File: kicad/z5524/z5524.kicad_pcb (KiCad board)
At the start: 4 copper layers, 80 x 80 mm, 210 parts, among them J1 Conn_01x01, J2 Conn_01x02, J3 Conn_02x20_Odd_Even, Q1 2N7002K, U1 TL074, U10 TL072, U11 NE5532, U12 TL074, U13 AS3364, U14 AD5328, U15 M24C02-WMN, U16 SSI2130, U17 DG442xY, U18 TL072, U19 LM311, U2 LM337L_TO92, U21 AD5328, U3 LM4040BIM3-2.5, U4 LM4040BIM3-4.1, U5 DG442xY, U6 TL072, U7 PCA9555D, U8 LM78L05_TO92, U9 AS3394

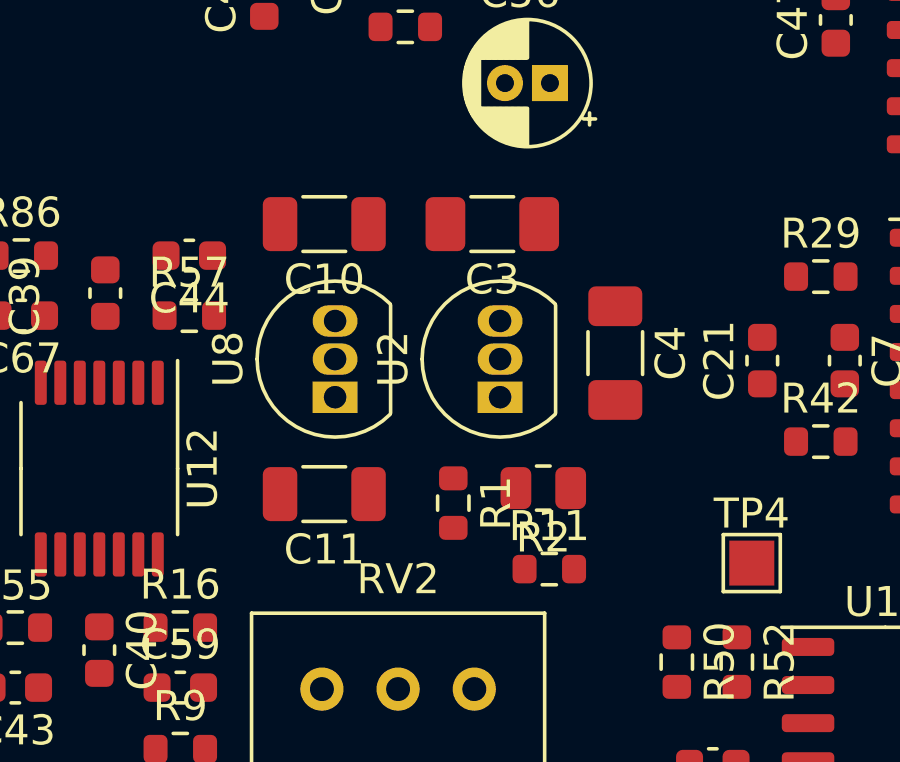
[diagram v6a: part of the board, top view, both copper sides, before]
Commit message: change some nets
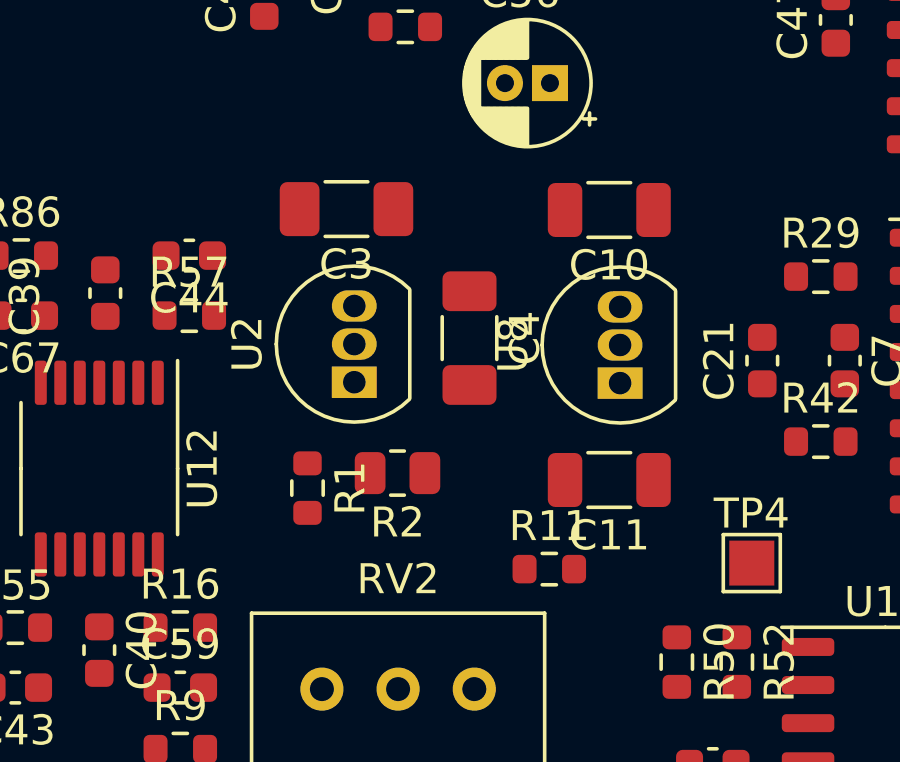
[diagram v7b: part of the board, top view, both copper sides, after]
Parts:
- moved C10 9.51 mm to (102.4, 53.4)
- moved C11 9.51 mm to (102.4, 62.4)
- moved U8 9.51 mm to (102.8, 59.2)
- moved C3 4.89 mm to (93.6, 53.4)
- moved C4 4.89 mm to (97.7, 57.7)
- moved R1 4.89 mm to (92.3, 62.7)
- moved R2 4.89 mm to (95.3, 62.2)
- moved U2 4.89 mm to (93.9, 59.2)
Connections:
- U21 pad 10: /DAC 2130/PULSE_MIX_DAC -> /DAC 2130/AS3394_VCO_CV_DAC
- U21 pad 11: /DAC 2130/TRI_MIX_DAC -> /DAC 2130/AS3394_SINE_CV_DAC
- U21 pad 12: /DAC 2130/AS3394_VCO_CV_DAC -> /DAC 2130/PULSE_MIX_DAC
- U21 pad 13: /DAC 2130/AS3394_SINE_CV_DAC -> /DAC 2130/TRI_MIX_DAC
- U21 pad 4: /DAC 2130/PWM_DAC -> /DAC 2130/SAW_MIX_DAC
- U21 pad 5: /DAC 2130/SAW_MIX_DAC -> /DAC 2130/LINEAR_DAC
- U21 pad 6: /DAC 2130/LINEAR_DAC -> /DAC 2130/EXP_PITCH_DAC
- U21 pad 7: /DAC 2130/EXP_PITCH_DAC -> /DAC 2130/PWM_DAC
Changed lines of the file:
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@@
   )
   (footprint "Resistor_SMD:R_0603_1608Metric" (layer "F.Cu")
-    (at 97.2 63.2 -90)
+    (at 92.34 62.7 -90)
     (descr "Resistor SMD 0603 (1608 Metric), square (rectangular) end terminal, IPC_7351 nominal, (Body size source: IPC-SM-782 page 72, https://www.pcb-3d.com/wordpress/wp-content/uploads/ipc-sm-782a_amendment_1_and_2.pdf), generated with kicad-footprint-generator")
     (tags "resistor")
@@
       (net 7 "+5V") (pinfunction "VDD") (pintype "power_in"))
     (pad "4" smd roundrect (at -2.8625 -0.325) (size 1.475 0.4) (layers "F.Cu" "F.Paste" "F.Mask") (roundrect_rratio 0.25)
-      (net 106 "/DAC 2130/PWM_DAC") (pinfunction "VOUT_A") (pintype "output"))
+      (net 107 "/DAC 2130/SAW_MIX_DAC") (pinfunction "VOUT_A") (pintype "output"))
     (pad "5" smd roundrect (at -2.8625 0.325) (size 1.475 0.4) (layers "F.Cu" "F.Paste" "F.Mask") (roundrect_rratio 0.25)
-      (net 107 "/DAC 2130/SAW_MIX_DAC") (pinfunction "VOUT_B") (pintype "output"))
+      (net 145 "/DAC 2130/LINEAR_DAC") (pinfunction "VOUT_B") (pintype "output"))
     (pad "6" smd roundrect (at -2.8625 0.975) (size 1.475 0.4) (layers "F.Cu" "F.Paste" "F.Mask") (roundrect_rratio 0.25)
-      (net 145 "/DAC 2130/LINEAR_DAC") (pinfunction "VOUT_C") (pintype "output"))
+      (net 100 "/DAC 2130/EXP_PITCH_DAC") (pinfunction "VOUT_C") (pintype "output"))
     (pad "7" smd roundrect (at -2.8625 1.625) (size 1.475 0.4) (layers "F.Cu" "F.Paste" "F.Mask") (roundrect_rratio 0.25)
-      (net 100 "/DAC 2130/EXP_PITCH_DAC") (pinfunction "VOUT_D") (pintype "output"))
+      (net 106 "/DAC 2130/PWM_DAC") (pinfunction "VOUT_D") (pintype "output"))
     (pad "8" smd roundrect (at -2.8625 2.275) (size 1.475 0.4) (layers "F.Cu" "F.Paste" "F.Mask") (roundrect_rratio 0.25)
       (net 5 "/VREF_2.5") (pinfunction "VREF_ABCD") (pintype "input"))
@@
       (net 5 "/VREF_2.5") (pinfunction "VREF_EFGH") (pintype "input"))
     (pad "10" smd roundrect (at 2.8625 1.625) (size 1.475 0.4) (layers "F.Cu" "F.Paste" "F.Mask") (roundrect_rratio 0.25)
-      (net 108 "/DAC 2130/PULSE_MIX_DAC") (pinfunction "VOUT_E") (pintype "output"))
+      (net 155 "/DAC 2130/AS3394_VCO_CV_DAC") (pinfunction "VOUT_E") (pintype "output"))
     (pad "11" smd roundrect (at 2.8625 0.975) (size 1.475 0.4) (layers "F.Cu" "F.Paste" "F.Mask") (roundrect_rratio 0.25)
-      (net 109 "/DAC 2130/TRI_MIX_DAC") (pinfunction "VOUT_F") (pintype "output"))
+      (net 156 "/DAC 2130/AS3394_SINE_CV_DAC") (pinfunction "VOUT_F") (pintype "output"))
     (pad "12" smd roundrect (at 2.8625 0.325) (size 1.475 0.4) (layers "F.Cu" "F.Paste" "F.Mask") (roundrect_rratio 0.25)
-      (net 155 "/DAC 2130/AS3394_VCO_CV_DAC") (pinfunction "VOUT_G") (pintype "output"))
+      (net 108 "/DAC 2130/PULSE_MIX_DAC") (pinfunction "VOUT_G") (pintype "output"))
     (pad "13" smd roundrect (at 2.8625 -0.325) (size 1.475 0.4) (layers "F.Cu" "F.Paste" "F.Mask") (roundrect_rratio 0.25)
-      (net 156 "/DAC 2130/AS3394_SINE_CV_DAC") (pinfunction "VOUT_H") (pintype "output"))
+      (net 109 "/DAC 2130/TRI_MIX_DAC") (pinfunction "VOUT_H") (pintype "output"))
     (pad "14" smd roundrect (at 2.8625 -0.975) (size 1.475 0.4) (layers "F.Cu" "F.Paste" "F.Mask") (roundrect_rratio 0.25)
       (net 1 "GND") (pinfunction "GND") (pintype "power_in"))
@@
   )
   (footprint "Capacitor_SMD:C_1206_3216Metric" (layer "F.Cu")
-    (at 92.9 62.9 180)
+    (at 102.4 62.43 180)
     (descr "Capacitor SMD 1206 (3216 Metric), square (rectangular) end terminal, IPC_7351 nominal, (Body size source: IPC-SM-782 page 76, https://www.pcb-3d.com/wordpress/wp-content/uploads/ipc-sm-782a_amendment_1_and_2.pdf), generated with kicad-footprint-generator")
     (tags "capacitor")
@@
   )
   (footprint "Package_TO_SOT_THT:TO-92_Inline" (layer "F.Cu")
-    (at 98.76 59.67 90)
+    (at 93.9 59.17 90)
     (descr "TO-92 leads in-line, narrow, oval pads, drill 0.75mm (see NXP sot054_po.pdf)")
     (tags "to-92 sc-43 sc-43a sot54 PA33 transistor")
@@
   )
   (footprint "Resistor_SMD:R_0805_2012Metric" (layer "F.Cu")
-    (at 100.2 62.7 180)
+    (at 95.34 62.2 180)
     (descr "Resistor SMD 0805 (2012 Metric), square (rectangular) end terminal, IPC_7351 nominal, (Body size source: IPC-SM-782 page 72, https://www.pcb-3d.com/wordpress/wp-content/uploads/ipc-sm-782a_amendment_1_and_2.pdf), generated with kicad-footprint-generator")
     (tags "resistor")
@@
   )
   (footprint "Capacitor_SMD:C_1206_3216Metric_Pad1.33x1.80mm_HandSolder" (layer "F.Cu")
-    (at 102.6 58.2 -90)
+    (at 97.74 57.7 -90)
     (descr "Capacitor SMD 1206 (3216 Metric), square (rectangular) end terminal, IPC_7351 nominal with elongated pad for handsoldering. (Body size source: IPC-SM-782 page 76, https://www.pcb-3d.com/wordpress/wp-content/uploads/ipc-sm-782a_amendment_1_and_2.pdf), generated with kicad-footprint-generator")
     (tags "capacitor handsolder")
@@
   )
   (footprint "Capacitor_SMD:C_1206_3216Metric_Pad1.33x1.80mm_HandSolder" (layer "F.Cu")
-    (at 98.5 53.9 180)
+    (at 93.64 53.4 180)
     (descr "Capacitor SMD 1206 (3216 Metric), square (rectangular) end terminal, IPC_7351 nominal with elongated pad for handsoldering. (Body size source: IPC-SM-782 page 76, https://www.pcb-3d.com/wordpress/wp-content/uploads/ipc-sm-782a_amendment_1_and_2.pdf), generated with kicad-footprint-generator")
     (tags "capacitor handsolder")
@@
   )
   (footprint "Capacitor_SMD:C_1206_3216Metric" (layer "F.Cu")
-    (at 92.9 53.9 180)
+    (at 102.4 53.43 180)
     (descr "Capacitor SMD 1206 (3216 Metric), square (rectangular) end terminal, IPC_7351 nominal, (Body size source: IPC-SM-782 page 76, https://www.pcb-3d.com/wordpress/wp-content/uploads/ipc-sm-782a_amendment_1_and_2.pdf), generated with kicad-footprint-generator")
     (tags "capacitor")
@@
   )
   (footprint "Package_TO_SOT_THT:TO-92_Inline" (layer "F.Cu")
-    (at 93.26 59.67 90)
+    (at 102.76 59.2 90)
     (descr "TO-92 leads in-line, narrow, oval pads, drill 0.75mm (see NXP sot054_po.pdf)")
     (tags "to-92 sc-43 sc-43a sot54 PA33 transistor")
@@
     )
   )
-  (group "" (id 2e246520-0b35-4792-ad25-97c2cddefbe2)
-    (members
-      92f9a68e-9e7e-466e-adbc-94ab08e4af57
-      d10bf185-8b68-491f-b0f1-91ced90c7d42
-    )
-  )
   (group "" (id 2fc85357-0847-4fe7-82a9-7b85cf4b86a6)
     (members
@@
     )
   )
-  (group "" (id 92f9a68e-9e7e-466e-adbc-94ab08e4af57)
+  (group "" (id 93d75bed-71db-44f9-b7da-dd2ff35bd6cd)
     (members
+      08c4fd51-5f1c-4dfa-ace4-9c1df0a83a9a
+      1761795b-03b3-4d1e-8c44-8f3a77735186
+      20aa8d9d-5e11-4ec8-bebb-96b6d7a66299
+      2b323b7b-dfb0-436f-9734-156e416652d1
+      32a03971-95b1-4e62-b42b-e4e30dc06bc9
       37a2353b-544e-489e-a308-03e152b14909
+      5a9364b0-aa06-471d-94c5-cc73b693e1fa
+      67ac6900-552f-4c0c-853a-365d1478a354
+      74f91626-498a-4694-b751-c8c8d0c3ce85
+      7aefe85a-953d-4bf9-832c-796f0bb3e17d
+      8c7152cb-4b92-4948-843e-82d814edd414
+      8d9b79bc-f815-4bc3-ab31-782ebc6dd427
+      a4beb0db-c2ca-4bc9-9f16-708ecfff1011
+      ad7e7393-7ac2-4a7d-805d-c9c501d4594d
+      b738d7b2-3c4e-413f-bd83-e0ed3588a6b0
       c147fb3d-f9dd-4c71-947d-6ad22714737b
       d7e2999d-533c-4dbd-8e1a-87664fb62fcd
@@
     )
   )
-  (group "" (id d10bf185-8b68-491f-b0f1-91ced90c7d42)
-    (members
-      08c4fd51-5f1c-4dfa-ace4-9c1df0a83a9a
-      1761795b-03b3-4d1e-8c44-8f3a77735186
-      20aa8d9d-5e11-4ec8-bebb-96b6d7a66299
-      2b323b7b-dfb0-436f-9734-156e416652d1
-      32a03971-95b1-4e62-b42b-e4e30dc06bc9
-      5a9364b0-aa06-471d-94c5-cc73b693e1fa
-      67ac6900-552f-4c0c-853a-365d1478a354
-      74f91626-498a-4694-b751-c8c8d0c3ce85
-      7aefe85a-953d-4bf9-832c-796f0bb3e17d
-      8c7152cb-4b92-4948-843e-82d814edd414
-      8d9b79bc-f815-4bc3-ab31-782ebc6dd427
-      a4beb0db-c2ca-4bc9-9f16-708ecfff1011
-      ad7e7393-7ac2-4a7d-805d-c9c501d4594d
-      b738d7b2-3c4e-413f-bd83-e0ed3588a6b0
-    )
-  )

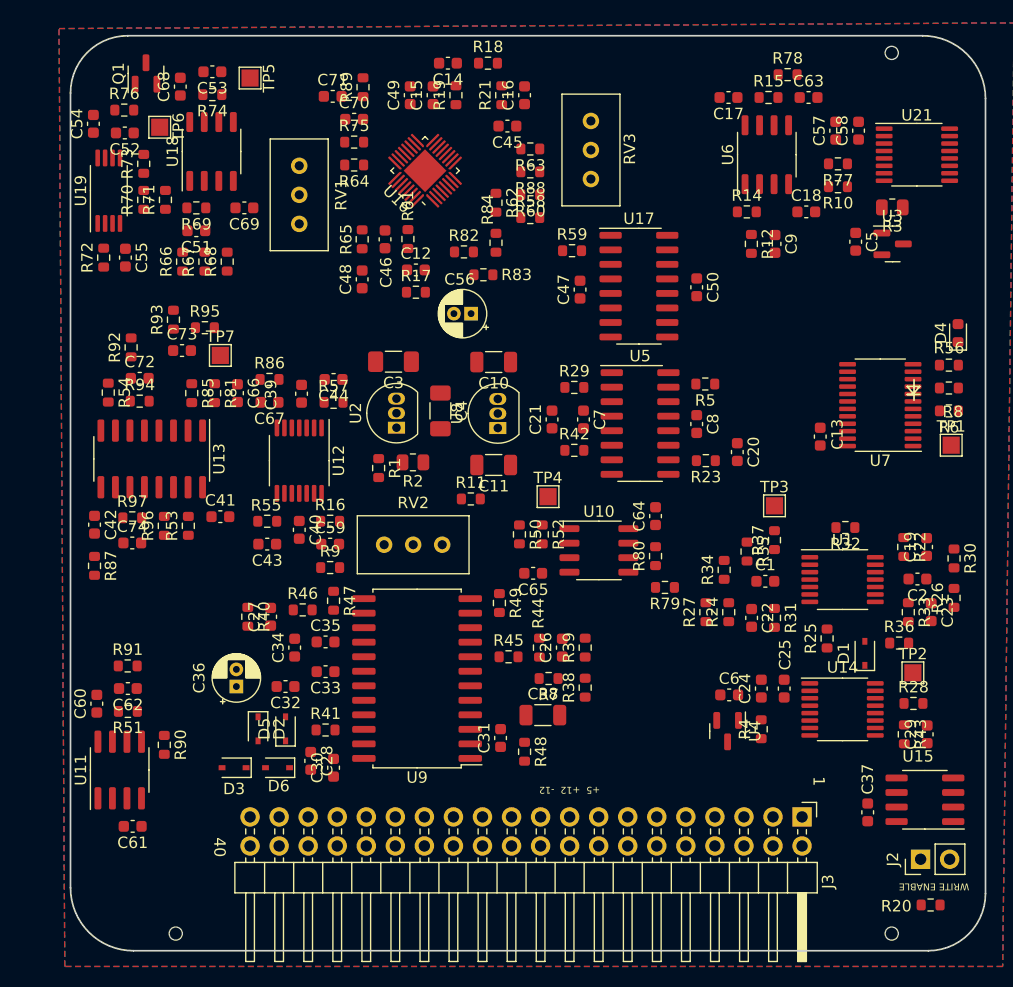
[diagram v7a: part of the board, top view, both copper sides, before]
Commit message: start routing power
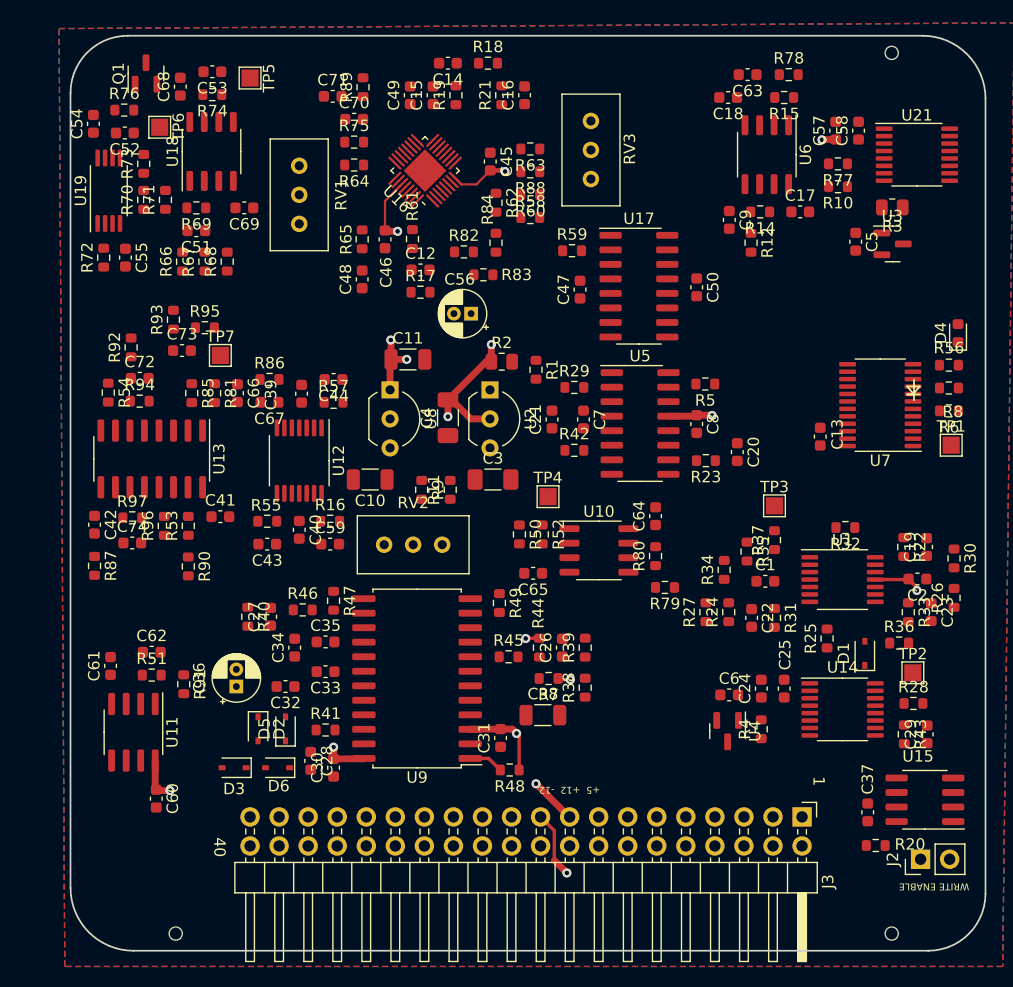
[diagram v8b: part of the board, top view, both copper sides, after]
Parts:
- U2, U8: footprint Package_TO_SOT_THT:TO-92_Inline -> Package_TO_SOT_THT:TO-92_Inline_Wide
- moved R1 16.2 mm to (106.1, 54.1)
- moved R90 15.7 mm to (75.7, 71.3)
- moved C10 14.9 mm to (91.6, 63.7)
- moved C61 14.2 mm to (68.9, 80.0), turned to 90 degrees
- moved C3 13.5 mm to (102.3, 63.7), turned to 0 degrees
- moved C18 12.1 mm to (122.9, 30.3), turned to 180 degrees
- moved C11 11.9 mm to (94.9, 53.2), turned to 0 degrees
- moved C17 11.8 mm to (129.2, 40.3), turned to 0 degrees
- moved R2 11.7 mm to (103.1, 53.4), turned to 0 degrees
- moved R9 10.5 mm to (96.1, 64.6), turned to -90 degrees
- moved U8 9.99 mm to (93.3, 55.9), turned to -90 degrees
- moved C60 9.79 mm to (72.9, 91.6), turned to -90 degrees
- moved U2 8.82 mm to (102.1, 55.9), turned to -90 degrees
- moved R20 7.08 mm to (135.8, 95.7), turned to 0 degrees
- moved C63 5.69 mm to (124.6, 28.3), turned to 180 degrees
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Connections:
- U11 pad 1: Net-(U11-Pad1) -> /AS3394_VCA
- U11 pad 2: Net-(U11-Pad1) -> /AS3394/VCA_OUTPUT
- U11 pad 6: /AS3394/VCA_OUTPUT -> Net-(U11-Pad6)
- U11 pad 7: /AS3394_VCA -> Net-(U11-Pad6)
- U6 pad 1: /DAC 2130/EXP_PITCH_2130 -> /DAC 2130/LINEAR_2130
- U6 pad 2: Net-(R12-Pad1) -> Net-(R15-Pad2)
- U6 pad 3: Net-(C9-Pad1) -> Net-(C63-Pad1)
- U6 pad 5: Net-(C63-Pad1) -> Net-(C9-Pad1)
- U6 pad 6: Net-(R15-Pad2) -> Net-(R12-Pad1)
- U6 pad 7: /DAC 2130/LINEAR_2130 -> /DAC 2130/EXP_PITCH_2130
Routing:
- net -12V: track 0.00 -> 173.7 mm, vias 0 -> 2
- net +12V: track 0.00 -> 148.8 mm, vias 0 -> 3
- net +5VA: track 0.00 -> 61.8 mm, vias 0 -> 4
- net -6V: track 0.00 -> 58.4 mm, vias 0 -> 6
- net Net-(R48-Pad2): track 0.00 -> 3.05 mm
- net +5V: track 0.00 -> 1.21 mm, vias 0 -> 1
- added copper zone on In2.Cu, net +12V
- added copper zone on In2.Cu, net -12V
- added copper zone on In2.Cu, net -6V
